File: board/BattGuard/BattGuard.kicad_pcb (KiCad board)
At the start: 4 copper layers, 160 x 80 mm, 156 parts, among them J1 OQ0271510000G, J10 Conn_01x01_Pin, J11 Conn_01x01_Pin, J12 Conn_01x01_Pin, J13 Conn_01x01_Pin, J14 Conn_01x01_Pin, J15 Conn_01x01_Pin, J17 S5B-XH-A, J2 Barrel_Jack, J3 Conn_01x22_Pin, J4 Conn_01x22_Pin, J5 Conn_01x02_Pin(xt60), J7 EC5 JUMP CONNECTOR, J8 GSB4111312HR, J9 Conn_01x01_Pin, Q1 SIR680LDP-T1-RE3, Q2 SIR680LDP-T1-RE3, Q3 SIR680LDP-T1-RE3, Q4 SIR680LDP-T1-RE3, Q7 AO3401A, Q8 2N7002, Q9 AO3401A, U1 BQ25756ERRVR, U2 LMR51420XDDCR, U3 MCP45HV51-ST, U4 INA226, U5 LM317_TO3, U6 TLV76133KVUR, U7 TLV61047DDC

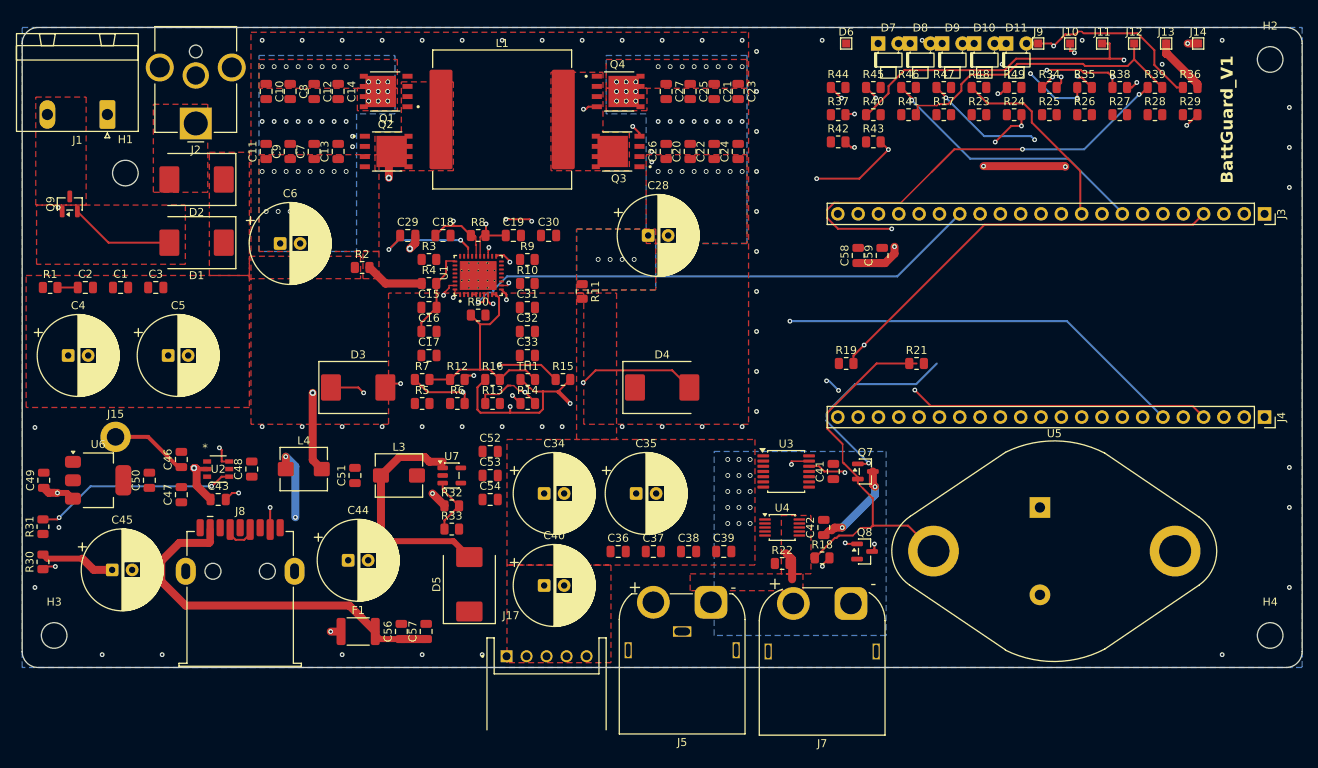
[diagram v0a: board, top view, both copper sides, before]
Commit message: 10.29.2026
fixed copper keepouts around all 4 mounting holes so the screws can’t short to the frame.
Removed J7 from the board,
Added fan pads J18 and J19
fixed polarized symbols
Changed C2 to 2.2 µF, 100 V, 1206.
BQ25756 Shifted according to checklist
Gave D3/D4 their correct small footprint.
Connected U1’s thermal vias to GND.
Re-routed the BQ area to the TI checklist:
HIDRV is 0.5 mm, paired with its SW trace.
LODRV runs on the bottom layer.
Fixed input nodes solar in, then solar_Prot(reverse protected node), and barrel in all to VCC node
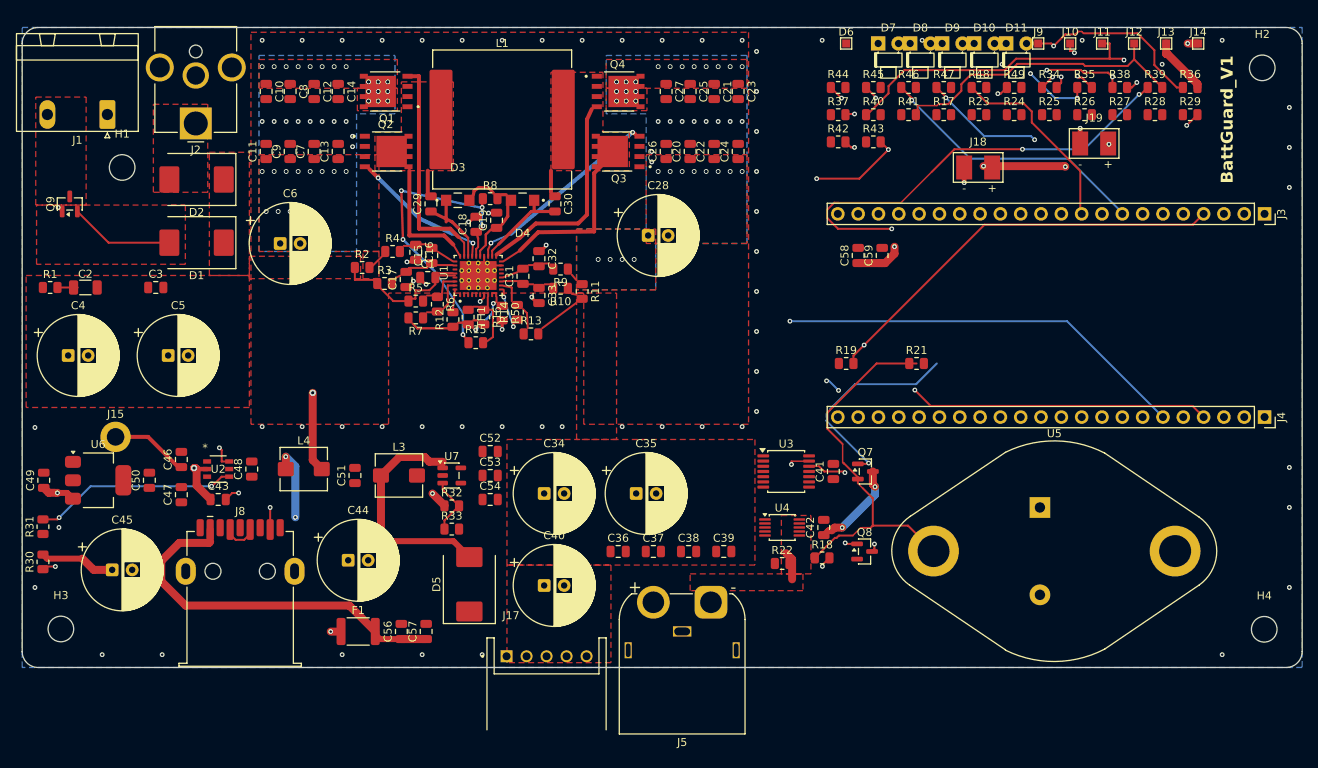
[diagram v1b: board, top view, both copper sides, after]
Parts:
- removed J7: EC5 JUMP CONNECTOR, Connector_AMASS:AMASS_XT60PW-M_1x02_P7.20mm_Horizontal
- added J18: FAN1 5V, TeamLib:Fan_Wire_Pads_1x02_SMD, F.Cu at (219.5, 67.5)
- added J19: FAN2 5V, TeamLib:Fan_Wire_Pads_1x02_SMD, F.Cu at (234.0, 64.5)
- C2: value 100 uF -> 2.2uF 100V; footprint Capacitor_SMD:C_0805_2012Metric -> Capacitor_SMD:C_1206_3216Metric
- D3, D4: footprint Diode_SMD:D_SMC -> TeamLib:DIO_V1FM10-M3_H
- moved C1 38.4 mm to (150.7, 81.2)
- moved D4 29.2 mm to (162.6, 71.6), turned to 180 degrees
- moved D3 26.5 mm to (154.4, 71.6)
- moved R5 12.8 mm to (149.2, 84.2)
- moved R6 12.6 mm to (151.9, 84.6), turned to -90 degrees
- moved R15 11.8 mm to (156.7, 89.4)
- moved R14 11.5 mm to (161.9, 85.6), turned to 90 degrees
- moved TH1 10.8 mm to (155.8, 86.2), turned to -90 degrees
- moved C16 10.0 mm to (149.2, 78.1), turned to -90 degrees
- moved R13 9.94 mm to (163.6, 88.3)
- moved C17 9.92 mm to (148.0, 81.5), turned to 90 degrees
- moved C32 9.21 mm to (164.6, 78.9), turned to -90 degrees
- moved R16 7.88 mm to (157.7, 86.2), turned to -90 degrees
- moved R7 7.74 mm to (149.2, 86.3), turned to 180 degrees
- moved C33 7.64 mm to (164.6, 83.5), turned to -90 degrees
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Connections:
- net Net-(D2-Pad2) renamed /BARREL_IN
- net Net-(Q9-S) renamed /SOLAR_PROT
- C1 pad 2: VAC -> VCC
- C3 pad 1: VAC -> VCC
- C4 pad 1: VAC -> VCC
- C5 pad 1: VAC -> VCC
- D1 pad 1: VAC -> VCC
- D2 pad 1: VAC -> VCC
- J1 pad 2: VCC -> /SOLAR_IN
- J3 pad 18: /GPIO11 -> /GPIO12
- J3 pad 19: /GPIO11 -> /GPIO13
- J3 pad 20: /GPIO11 -> /GPIO14
- Q9 pad 3: VCC -> /SOLAR_IN
- R1 pad 1: VAC -> VCC
- R2 pad 1: VAC -> VCC
- R26 pad 2: /GPIO11 -> /GPIO12
- R27 pad 2: /GPIO11 -> /GPIO13
- R28 pad 2: /GPIO11 -> /GPIO14
- R3 pad 1: VAC -> VCC
- R5 pad 1: VAC -> VCC
- U1 pad 32: VAC -> VCC
- U1 pad 33: VAC -> VCC
- U1 pad 4: /GPIO11 -> /GPIO12
- U1 pad 5: /GPIO11 -> /GPIO13
- U4 pad 3: /GPIO11 -> /GPIO14
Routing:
- net /GPIO10: track 82.9 -> 1.06 mm, vias 3 -> 1
- net Net-(U1-DRV_SUP): track 77.6 -> 10.3 mm, vias 3 -> 0
- net /TS: track 40.6 -> 6.60 mm, vias 3 -> 0
- net /HIDRV1: track 0.00 -> 28.6 mm
- net Net-(U1-BTST1): track 37.8 -> 10.8 mm, vias 3 -> 0
- net /SW2: track 0.00 -> 26.3 mm
- net Net-(U1-FB): track 24.5 -> 5.33 mm, vias 2 -> 0
- net Net-(U1-ACOV): track 23.5 -> 4.91 mm, vias 2 -> 0
- net VCC: track 0.00 -> 18.0 mm
- net /LODRV1: track 0.00 -> 17.5 mm, vias 0 -> 2
- net AGND: track 28.5 -> 11.7 mm, vias 0 -> 2
- net /BTST2: track 0.00 -> 12.0 mm
- net Net-(U1-FSW_SYNC): track 13.3 -> 2.46 mm, vias 2 -> 0
- net /FBG: track 15.2 -> 5.19 mm
- net GND: track 3.82 -> 13.9 mm, vias 78 -> 88
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- added copper zone on F.Cu, net /SOLAR_IN
- removed copper zone on B.Cu, net /Vsystem

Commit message: ESD Protection Diodes + 60V 6.6A PMOS RV Prot
Updated schematic and layout to include 15V and 5V ESD protection diodes to the charge output. Also replaced undersized PMOS for solar reverse voltage input with 8-pin DIP DGS PMOSFET.
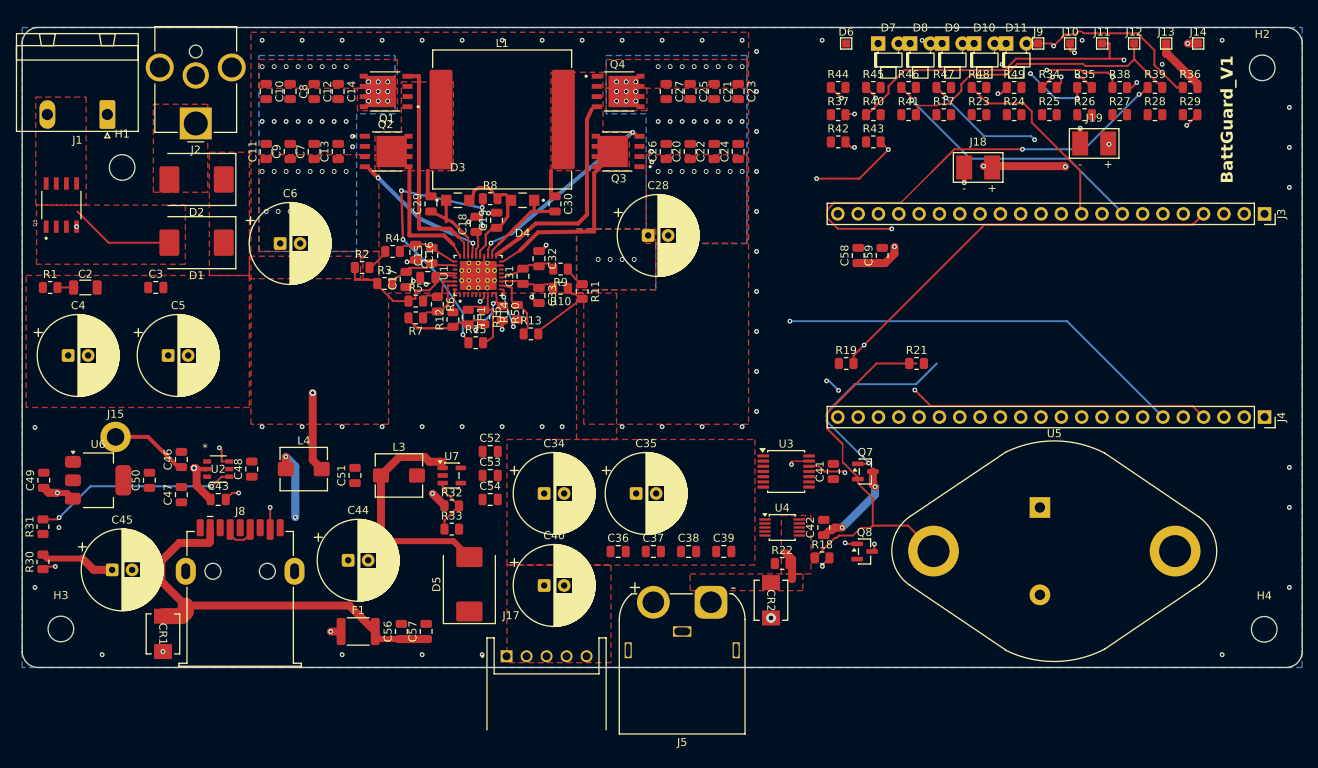
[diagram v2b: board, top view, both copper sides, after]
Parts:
- removed Q9: AO3401A, Package_TO_SOT_SMD:SOT-23
- added CR1: SMBJ5.0A, TeamLib:DO-214AASMB_J-BEND_LTF, F.Cu at (117.6, 125.8)
- added CR2: SMBJ15A, TeamLib:DO-214AASMB_J-BEND_LTF, F.Cu at (193.6, 121.6)
- added Q5: Q_PMOS_DGS, TeamLib:SOIC127P600X175-8N, F.Cu at (104.9, 72.2)
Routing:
- net Net-(J8-VBUS): track 47.5 -> 51.4 mm
- net GND: track 13.9 -> 12.8 mm, vias 88 -> 89

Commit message: 10.29.2026
Fixed pad connections around BQ, moved Thermisistor pads and setup vias for wires, keepout for inductor, placed oled header connector,
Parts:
- removed TH1: 10k, Resistor_SMD:R_0805_2012Metric
- added J6: OLED DISPLAY, Connector_PinHeader_2.54mm:PinHeader_1x05_P2.54mm_Vertical, F.Cu at (254.6, 61.3)
- C4, C5: value 56uF -> 56uF 80v
- moved R50 6.74 mm to (159.4, 92.4)
- moved R16 6.49 mm to (156.1, 92.5)
- moved R15 5.60 mm to (152.1, 92.6), turned to -90 degrees
- moved J3 2.54 mm to (255.3, 75.8)
- moved R13 0.89 mm to (164.5, 88.3)
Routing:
- net /GPIO4: track 81.2 -> 31.9 mm
- net AGND: track 11.7 -> 28.7 mm
- net /SOLAR_PROT: track 13.1 -> 0.00 mm
- net /SW1: track 18.5 -> 28.9 mm
- net /TS: track 6.60 -> 16.3 mm, vias 0 -> 1
- net /SW2: track 26.3 -> 34.5 mm
- net /REGN: track 37.4 -> 43.6 mm
- net Net-(U1-SRP): track 3.00 -> 7.63 mm
- net Net-(J8-D+): track 4.24 -> 8.40 mm
- net /Vsystem: track 15.8 -> 19.2 mm
- net Net-(U1-ACN): track 3.65 -> 6.67 mm
- net Net-(U1-FB): track 5.33 -> 8.30 mm
- net /GPIO18: track 45.9 -> 48.4 mm
- net /GPIO15: track 34.4 -> 37.0 mm
- net /GPIO7: track 15.2 -> 17.8 mm
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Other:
- board text added: "TH1"

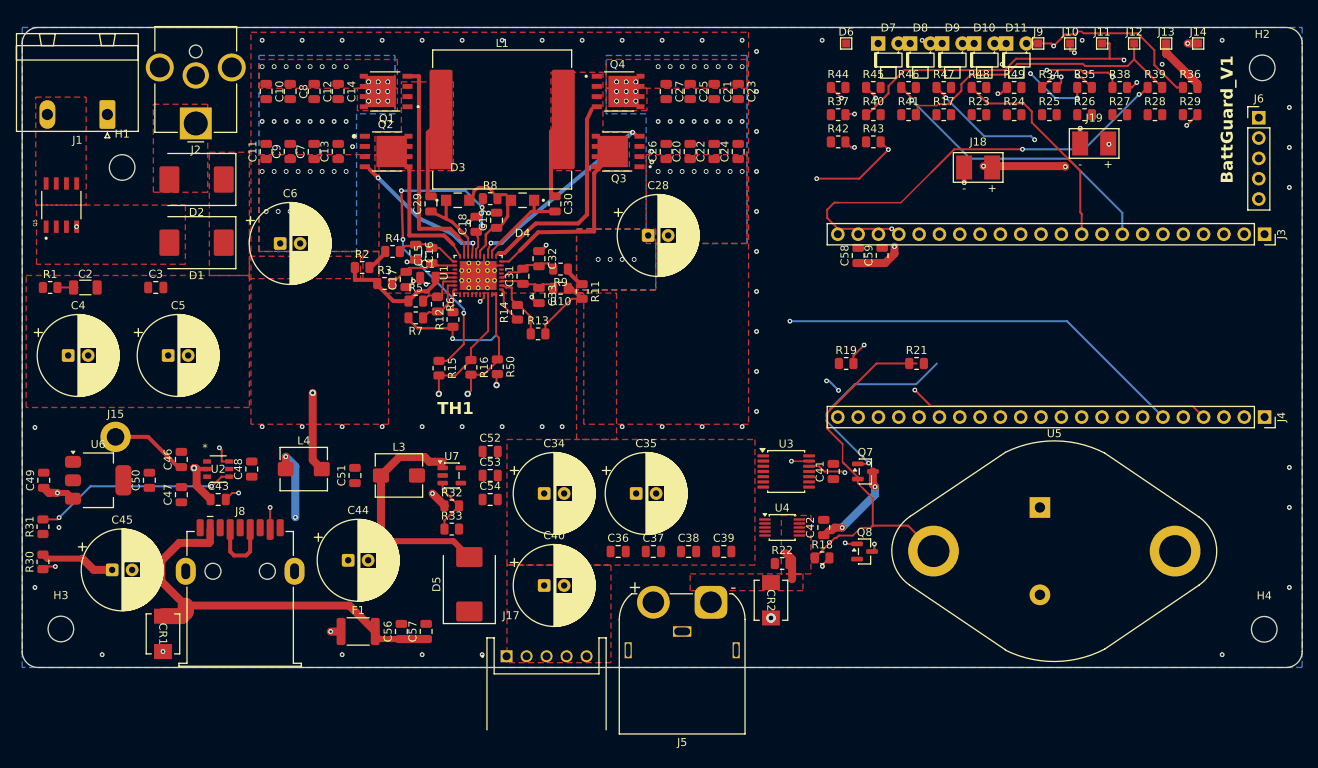
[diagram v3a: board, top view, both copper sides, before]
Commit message: 10.29.2026 Night
Routed ALL GPIO Traces from bq and other perhpirals, moved fan pads to oppsite sides of boards, fixed LED pads,
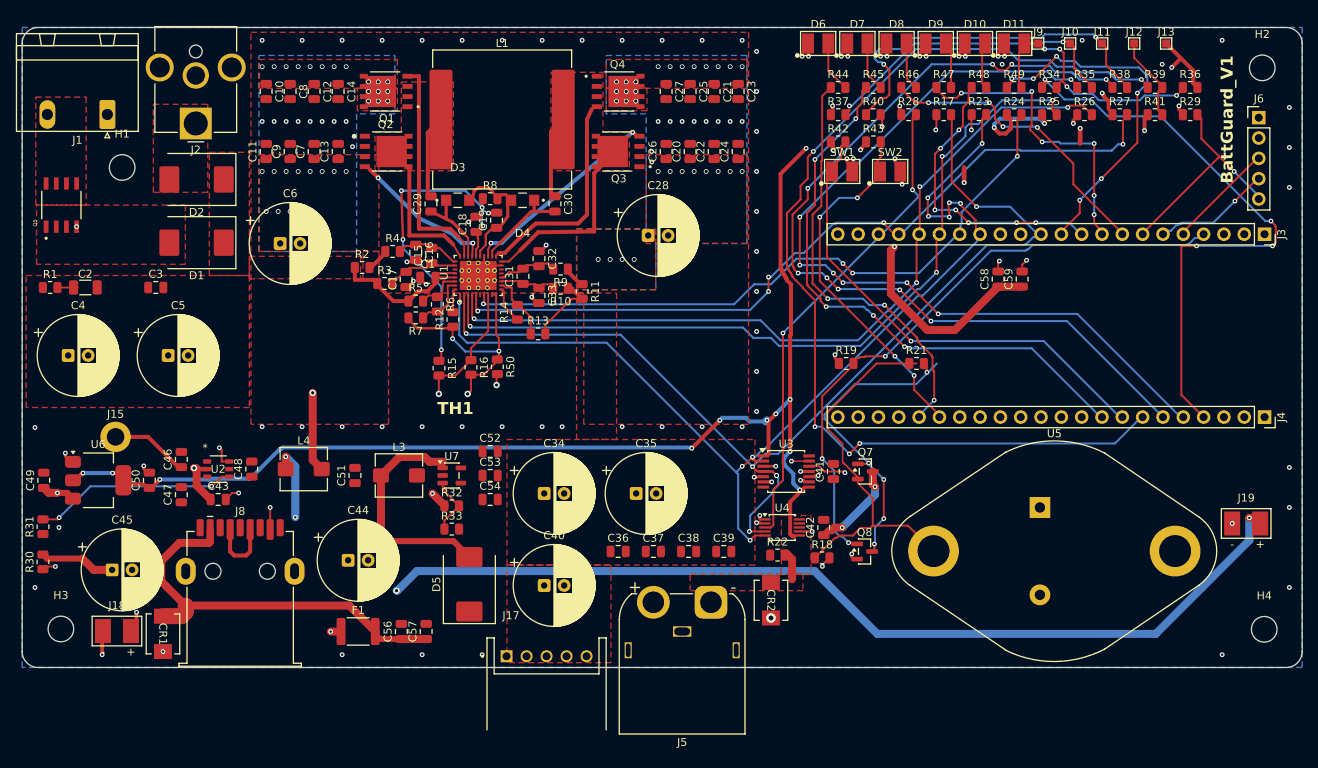
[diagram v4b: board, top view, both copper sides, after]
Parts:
- removed J14: Conn_01x01_Pin, TestPoint:TestPoint_Pad_1.0x1.0mm
- added SW1: SW_Push, TeamLib:Wire_Pads_1x02_SMD_2.54, F.Cu at (202.5, 68.0)
- added SW2: SW_Push, TeamLib:Wire_Pads_1x02_SMD_2.54, F.Cu at (208.5, 68.0)
- D10, D11, D7, D8, D9: footprint LED_THT:LED_D1.8mm_W1.8mm_H2.4mm_Horizontal_O1.27mm_Z4.9mm -> TeamLib:Wire_Pads_1x02_SMD_2.54
- D6: footprint TestPoint:TestPoint_Pad_1.0x1.0mm -> TeamLib:Wire_Pads_1x02_SMD_2.54
- moved J18 122.3 mm to (111.8, 125.5)
- moved J19 51.2 mm to (253.0, 112.0)
- moved R28 30.8 mm to (210.8, 60.9)
- moved R41 30.8 mm to (241.6, 60.9)
- moved C58 17.7 mm to (222.0, 81.5)
- moved C59 17.7 mm to (225.0, 81.5)
- moved D6 3.50 mm to (199.5, 52.0)
- moved D7 2.60 mm to (204.4, 52.0)
- moved D8 1.70 mm to (209.3, 52.0)
- moved R22 1.20 mm to (194.4, 116.0)
- moved D11 1.00 mm to (224.0, 52.0)
- moved D9 0.80 mm to (214.2, 52.0)
- moved D10 0.10 mm to (219.1, 52.0)
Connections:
- J3 pad 1: Net-(J3-Pin_1) -> +3V3
- J3 pad 2: Net-(J3-Pin_1) -> +3V3
- J3 pad 21: +5V -> unconnected-(J3-Pin_21-Pad21)
- J6 pad 2: /3v3 -> +3V3
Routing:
- net +3V3: track 7.22 -> 180.0 mm, vias 0 -> 25
- net /GPIO8: track 0.00 -> 127.9 mm, vias 0 -> 6
- net /GPIO9: track 0.00 -> 127.4 mm, vias 0 -> 10
- net /GPIO11: track 0.00 -> 99.3 mm, vias 0 -> 4
- net /GPIO12: track 0.00 -> 98.9 mm, vias 0 -> 4
- net /GPIO13: track 0.00 -> 94.7 mm, vias 0 -> 5
- net +5V: track 93.3 -> 176.0 mm, vias 9 -> 8
- net /GPIO10: track 1.06 -> 82.0 mm, vias 1 -> 4
- net /GPIO14: track 0.00 -> 58.3 mm, vias 0 -> 2
- net /GPIO4: track 31.9 -> 73.9 mm, vias 2 -> 3
- net /GPIO2: track 144.1 -> 104.1 mm, vias 2 -> 7
- net /GPIO1: track 109.4 -> 74.3 mm, vias 2 -> 4
- net /GPIO16: track 71.3 -> 36.4 mm, vias 2 -> 6
- net /GPIO41: track 97.2 -> 129.8 mm, vias 3 -> 5
- net Net-(J12-Pin_1): track 38.4 -> 10.8 mm
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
